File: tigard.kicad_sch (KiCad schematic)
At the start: 91 parts, among them J1 USB_C_Receptacle_USB2.0, J2 JTAG, J3 UART, J4 SPI, J5 CORTEX, J6 LA, J7 I2C, Q1 BSH103, SW1 TARGET, SW2 MODE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

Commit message: address all issues in #84
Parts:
- removed C25: NF, Capacitor_SMD:C_0402_1005Metric, symbol Device:C_Small
- removed R3: 1M, Resistor_SMD:R_0402_1005Metric, symbol Device:R_Small
- H1, H2, H3, H4, JP1, JP2, LOGO1, LOGO2: now left out of the parts list
- J1: LCSC C165948 -> C2927038; P/N TYPE-C-31-M-12 -> USB-TYPE-C-018
- J2: LCSC C358689 -> C492407; P/N MTP125-1108S1 -> PZ254V-11-08P
- J3: LCSC C492408 -> C41425312 or C41425299; P/N PZ254V-11-09P -> PZ254V-11-09P-RD or -YL
- J4: LCSC C358693 -> C42431809; P/N MTP125-1204S1 -> PZ2.54-2X4P-H25
- J6: Key (none) -> conn-th-01in-7-2-hdr; LCSC (none) -> C7465995
- J7: LCSC C160404 -> C7433425; P/N SM04B-SRSS-TB(LF)(SN) -> HCZZ0032-4
- SW1: LCSC C255514 -> C128960; P/N SSSS224100 -> K3-2410D-F1
- SW2: LCSC C221663 -> C2906278; P/N JS202011CQN -> MSS22D18G2 125
- TP1: LCSC C238122 -> C5199805; P/N 5001 -> RH-5115
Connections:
- net +1V8: now also SW1.4
- net +3V3: now also SW1.2
- net +5V: now also SW1.1
- net GND: now also J1.S1 (SHIELD), SW1.SHIELD (10)
- net VREF: now also SW1.3
- net VTARGET: now also SW1.5
- no-connect marks 30 -> 25

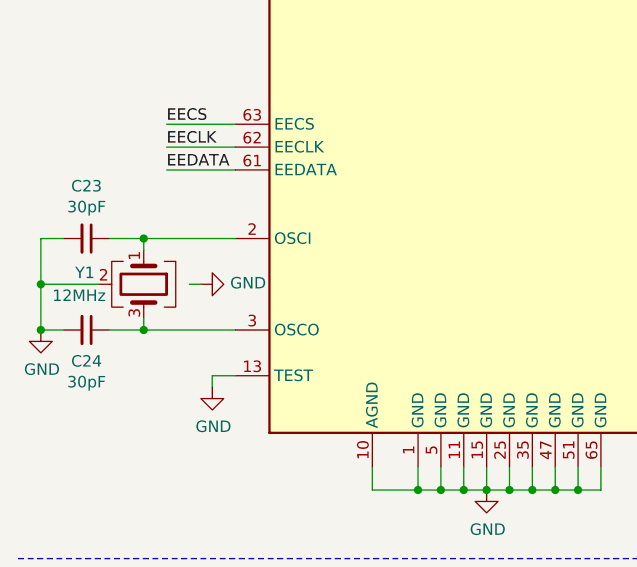
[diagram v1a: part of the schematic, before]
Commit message: Update part #s, track widths, and pour keepouts
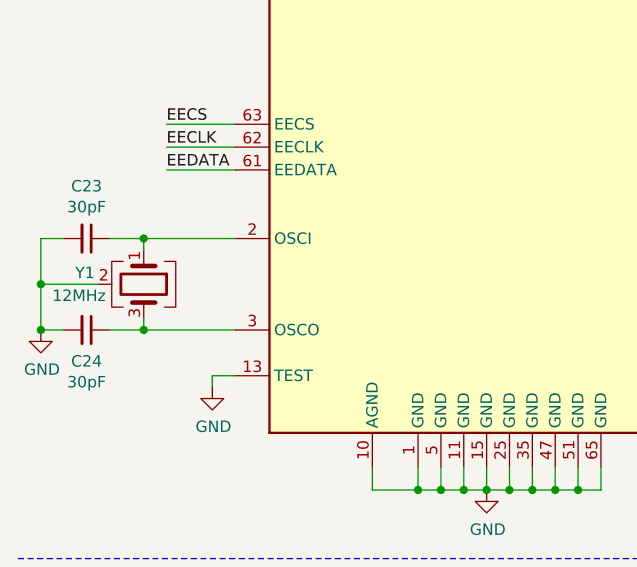
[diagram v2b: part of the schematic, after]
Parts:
- R10, R12, R13, R14, R18, R19, R20, R21, R24, R7: LCSC C301923 -> C25744; P/N 040200J0103TCE -> 0402WGF1002TCE
